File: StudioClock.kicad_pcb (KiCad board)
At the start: 2 copper layers, 100 x 100 mm, 80 parts, among them J1 CONN_01X16, J2 CONN_01X16, U1 7Seg_CA, U2 7Seg_CA, U3 7Seg_CA, U4 7Seg_CA

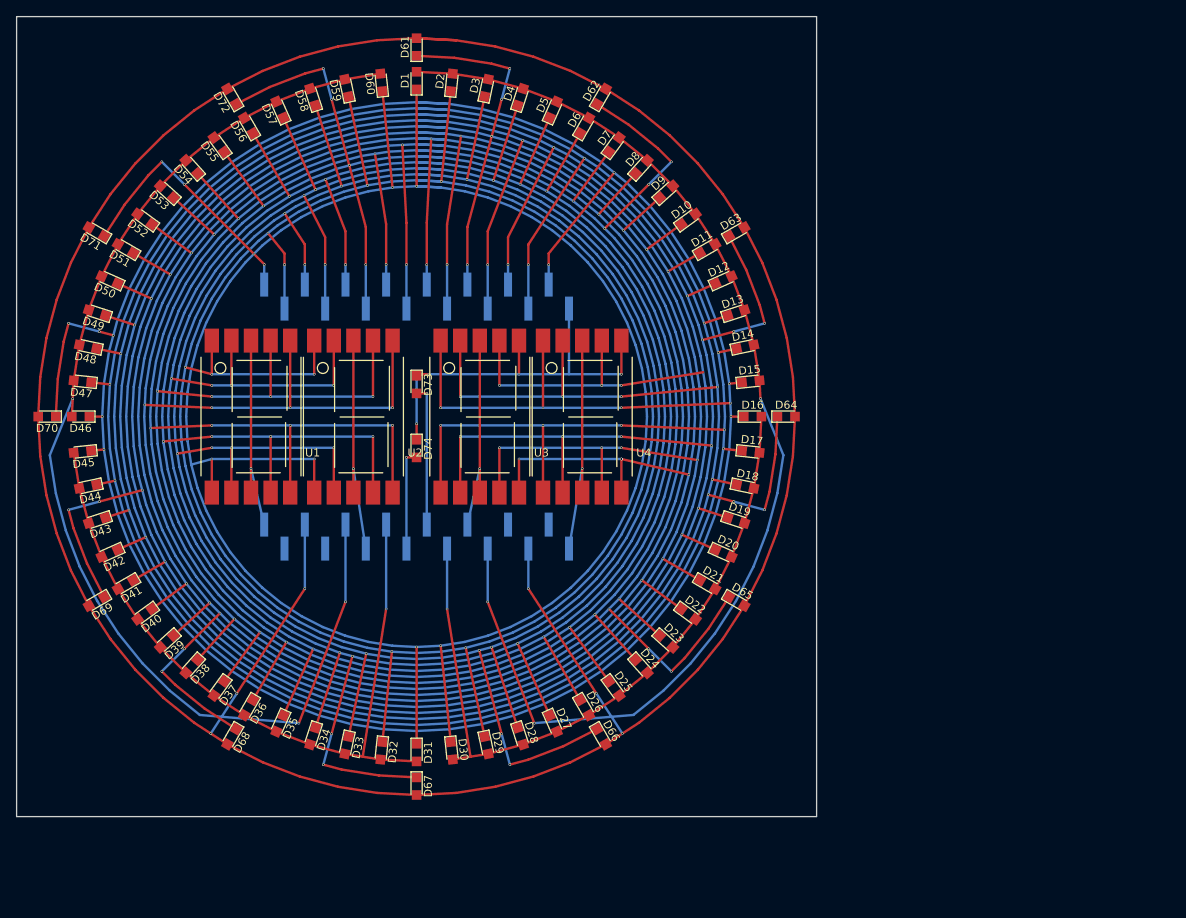
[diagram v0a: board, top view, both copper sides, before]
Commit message: script runs, updated symbols and footprints
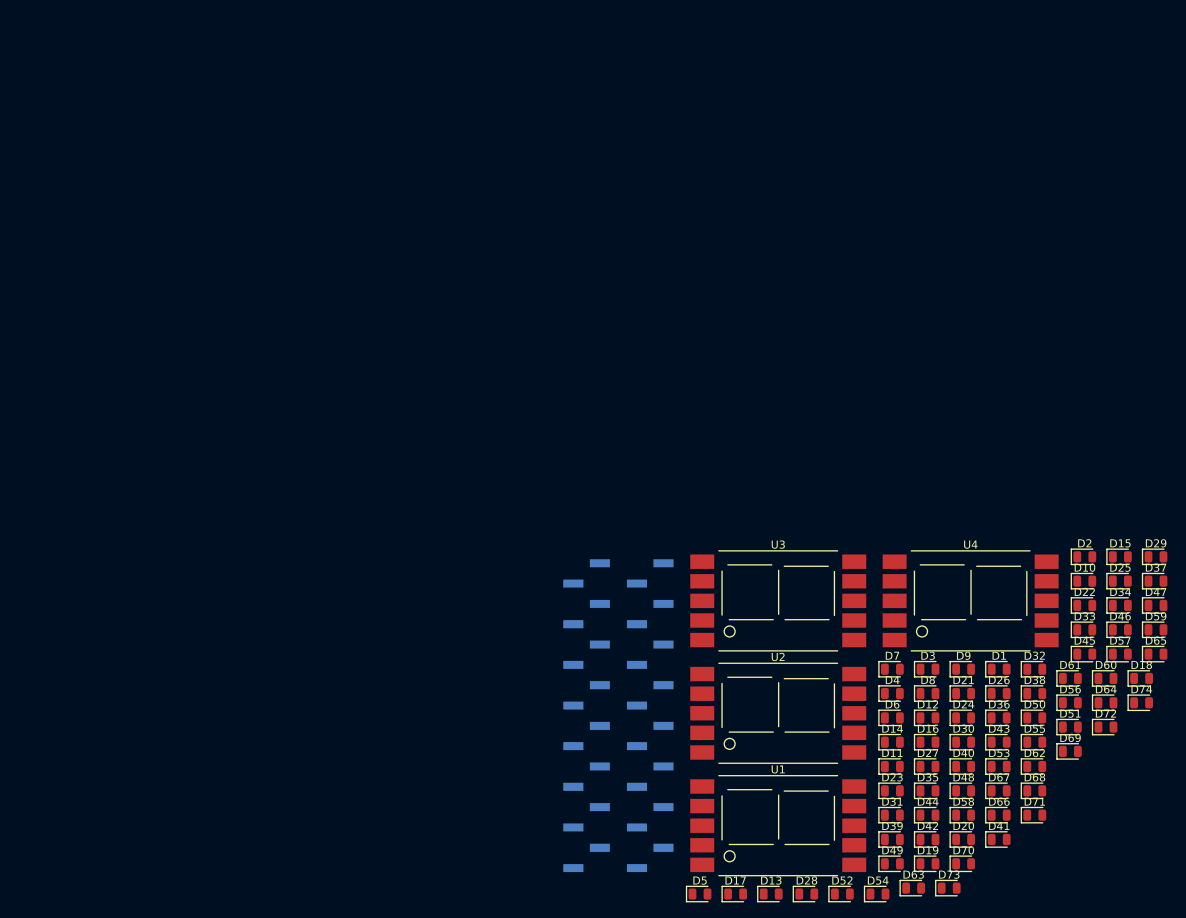
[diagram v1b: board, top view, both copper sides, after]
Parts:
- D1, D10, D11, D12, D13, D14, D15, D16, D17, D18, D19, D2, D20, D21, D22, D23, D24, D25, D26, D27, D28, D29, D3, D30, D31, D32, D33, D34, D35, D36, D37, D38, D39, D4, D40, D41, D42, D43, D44, D45, D46, D47, D48, D49, D5, D50, D51, D52, D53, D54, D55, D56, D57, D58, D59, D6, D60, D61, D62, D63, D64, D65, D66, D67, D68, D69, D7, D70, D71, D72, D73, D74, D8, D9: footprint LEDs:LED_0805 -> LED_SMD:LED_0805_2012Metric
- J1, J2: footprint Pin_Headers:Pin_Header_Straight_1x16_Pitch2.54mm_SMD_Pin1Left -> Connector_PinHeader_2.54mm:PinHeader_1x16_P2.54mm_Vertical_SMD_Pin1Left
- U1, U2, U3, U4: value 7Seg_CA -> 7SEGMENTS; footprint Displays_7-Segment:7SEGMENT-LED__HDSM531_HDSM533_SMD -> Display_7Segment:7SEGMENT-LED__HDSM531_HDSM533_SMD
- moved D71 138.1 mm to (77.3, 49.8), turned to 0 degrees
- moved D47 137.1 mm to (92.4, 23.6), turned to 0 degrees
- moved D72 134.7 mm to (86.2, 38.8), turned to 0 degrees
- moved D46 132.7 mm to (88.0, 26.7), turned to 0 degrees
- moved D51 132.4 mm to (81.7, 38.8), turned to 0 degrees
- moved D50 127.9 mm to (77.3, 37.7), turned to 0 degrees
- moved D45 127.8 mm to (83.5, 29.7), turned to 0 degrees
- moved D70 127.5 mm to (68.4, 55.9), turned to 0 degrees
- moved D53 126.4 mm to (72.8, 43.7), turned to 0 degrees
- moved D55 126.4 mm to (77.3, 40.7), turned to 0 degrees
- moved D56 125.5 mm to (81.7, 35.8), turned to 0 degrees
- moved D57 125.2 mm to (88.0, 29.7), turned to 0 degrees
- moved D54 125.0 mm to (57.7, 59.7), turned to 0 degrees
- moved D69 123.2 mm to (81.7, 41.9), turned to 0 degrees
- moved D48 122.7 mm to (68.4, 46.8), turned to 0 degrees
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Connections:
- J2 pad 13: Net-(J2-Pad13) -> (no net)
- J2 pad 15: Net-(J2-Pad15) -> (no net)
- J2 pad 2: Net-(J2-Pad2) -> (no net)
- J2 pad 4: Net-(J2-Pad4) -> (no net)
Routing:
- net /a4: track 358.2 -> 0.00 mm, vias 6 -> 0
- net /k14: track 344.8 -> 0.00 mm, vias 12 -> 0
- net /k11: track 339.1 -> 0.00 mm, vias 12 -> 0
- net /k12: track 337.6 -> 0.00 mm, vias 12 -> 0
- net /k7: track 335.9 -> 0.00 mm, vias 13 -> 0
- net /k6: track 330.1 -> 0.00 mm, vias 14 -> 0
- net /k13: track 328.7 -> 0.00 mm, vias 9 -> 0
- net /k9: track 327.5 -> 0.00 mm, vias 12 -> 0
- net /k10: track 326.5 -> 0.00 mm, vias 11 -> 0
- net /k5: track 324.7 -> 0.00 mm, vias 12 -> 0
- net /k8: track 316.8 -> 0.00 mm, vias 12 -> 0
- net /k3: track 309.8 -> 0.00 mm, vias 14 -> 0
- net /k2: track 302.9 -> 0.00 mm, vias 14 -> 0
- net /k4: track 293.3 -> 0.00 mm, vias 11 -> 0
- net /k0: track 288.6 -> 0.00 mm, vias 11 -> 0
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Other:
- board outline removed

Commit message: executed and cleaned up files, added README
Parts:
- moved D71 138.1 mm to (-40.0, -23.1), turned to 150 degrees
- moved D47 137.1 mm to (-41.8, -4.39), turned to 174 degrees
- moved D72 134.7 mm to (-23.1, -40.0), turned to 120 degrees
- moved D46 132.7 mm to (-42.0, 0.00), turned to 180 degrees
- moved D51 132.4 mm to (-36.4, -21.0), turned to 150 degrees
- moved D50 127.9 mm to (-38.4, -17.1), turned to 156 degrees
- moved D45 127.8 mm to (-41.8, 4.39), turned to 186 degrees
- moved D70 127.5 mm to (-46.2, 0.00), turned to 180 degrees
- moved D53 126.4 mm to (-31.2, -28.1), turned to 138 degrees
- moved D55 126.4 mm to (-24.7, -34.0), turned to 126 degrees
- moved D56 125.5 mm to (-21.0, -36.4), turned to 120 degrees
- moved D57 125.2 mm to (-17.1, -38.4), turned to 114 degrees
- moved D54 125.0 mm to (-28.1, -31.2), turned to 132 degrees
- moved D69 123.2 mm to (-40.0, 23.1), turned to 210 degrees
- moved D48 122.7 mm to (-41.1, -8.73), turned to 168 degrees
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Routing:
- net /a4: track 0.00 -> 370.6 mm, vias 0 -> 5
- net /k14: track 0.00 -> 345.4 mm, vias 0 -> 13
- net /k11: track 0.00 -> 340.0 mm, vias 0 -> 13
- net /k12: track 0.00 -> 338.2 mm, vias 0 -> 13
- net /k7: track 0.00 -> 336.8 mm, vias 0 -> 13
- net /k6: track 0.00 -> 330.7 mm, vias 0 -> 13
- net /k13: track 0.00 -> 329.4 mm, vias 0 -> 10
- net /k9: track 0.00 -> 328.4 mm, vias 0 -> 13
- net /k10: track 0.00 -> 327.1 mm, vias 0 -> 12
- net /k5: track 0.00 -> 325.6 mm, vias 0 -> 12
- net /k8: track 0.00 -> 317.4 mm, vias 0 -> 12
- net /k3: track 0.00 -> 310.7 mm, vias 0 -> 13
- net /k2: track 0.00 -> 303.5 mm, vias 0 -> 13
- net /k4: track 0.00 -> 293.7 mm, vias 0 -> 10
- net /k0: track 0.00 -> 289.2 mm, vias 0 -> 11
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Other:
- board outline added: 100 x 100 mm
